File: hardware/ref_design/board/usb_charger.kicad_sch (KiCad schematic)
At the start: 34 parts, among them J1 TYPE-C-31-M-12, J2 53261-0271, Q2 AO3401A, Q4 2N7002, U1 SRV05-4, U2 TP4056-42-ESOP8

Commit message: ref_design: U1 is hongjiacheng's SRV05-4A (C20615829), a Preferred part
Same pinout as Semtech's SRV05-4.TCT (C13612, Extended), 1.0 pF to GND, 15 kV contact and
air; drops a $3-an-order setup fee. pin_review/u1.json re-checked against its datasheet
(check_pins PASS); check_netlist PASS. The board needs no copper change.

Co-Authored-By: Claude Opus 5.5 <noreply@anthropic.com>
Claude-Session: https://claude.ai/code/session_01NxPKqL46d94oRzrtCbFjri
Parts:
- U1: LCSC C13612 -> C20615829; MPN SRV05-4.TCT -> SRV05-4A; Manufacturer Semtech -> Zhuhai Hongjiacheng
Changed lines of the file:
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@@
 			)
 		)
-		(property "LCSC" "C13612"
+		(property "LCSC" "C20615829"
 			(at 73.66 101.6 0)
 			(hide yes)
@@
 			)
 		)
-		(property "MPN" "SRV05-4.TCT"
+		(property "MPN" "SRV05-4A"
 			(at 73.66 101.6 0)
 			(hide yes)
@@
 			)
 		)
-		(property "Manufacturer" "Semtech"
+		(property "Manufacturer" "Zhuhai Hongjiacheng"
 			(at 73.66 101.6 0)
 			(hide yes)

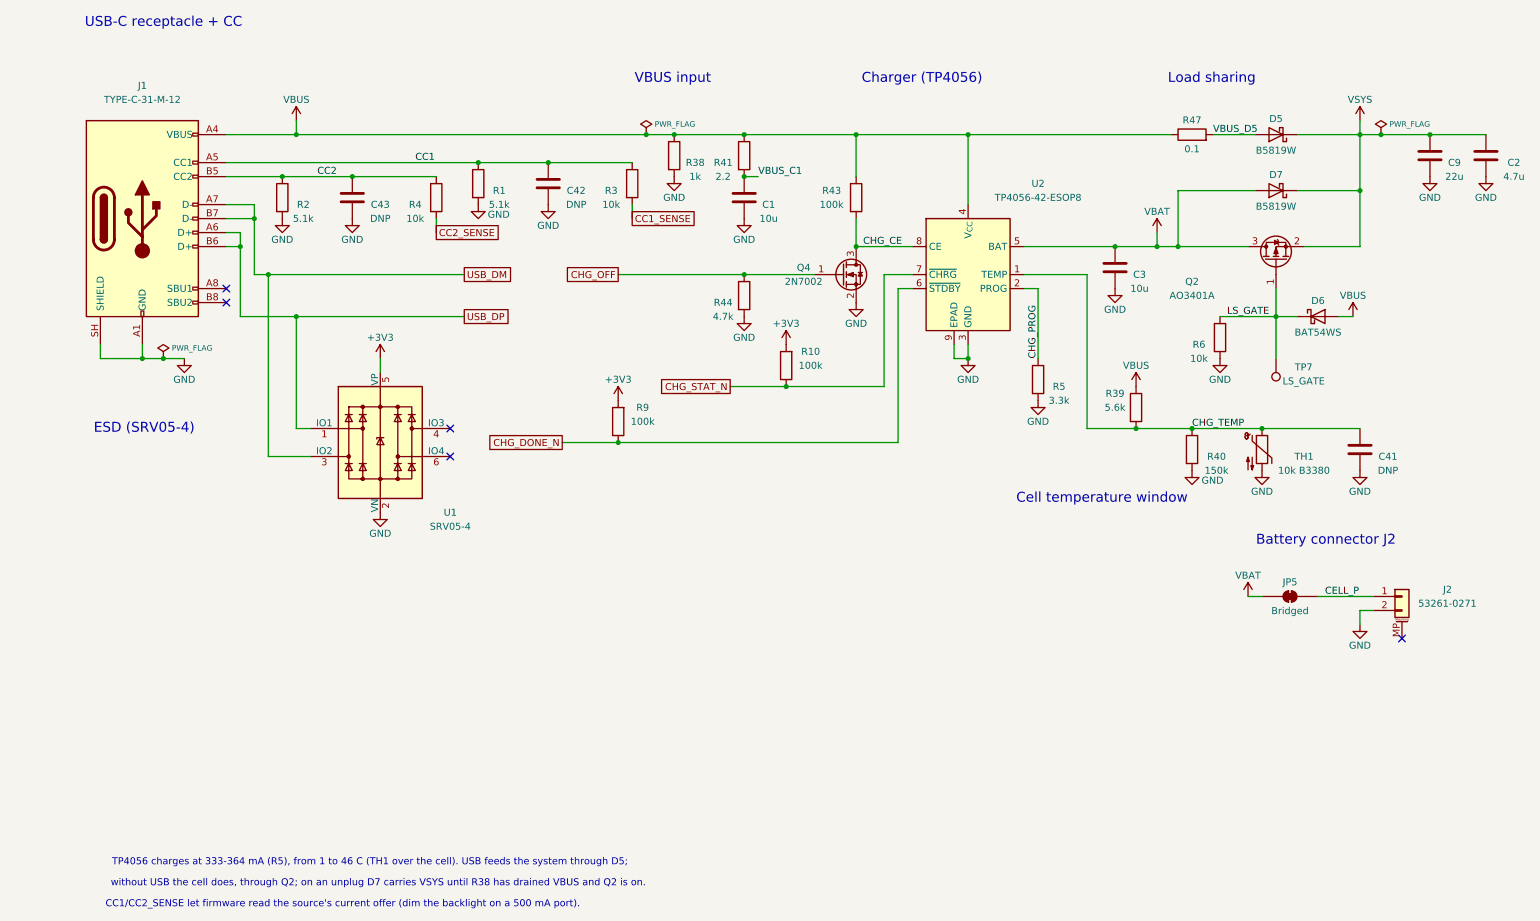
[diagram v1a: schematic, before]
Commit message: WIP: row 19 with shift registers and rows 1, 4, 16; 2 nets unrouted
The cell in a 54.0 x 37.0 mm hole, no speaker, every machine-placed part on
the top. New since the last WIP: each seat's D-pad and A/B/X/Y through a
74HC165 (SN74HC165PWR, chained, SR_PL/SR_CLK/SR_DATA on GPIO28-30, 10k
arrays); seat 2's Start powers on too (D8, R62, Q7, R63; P2_START on
GPIO34); Start/Select on 4 mm metal dome footprints; the BQ24073 power-path
charger in place of the TP4056 and its load sharing (pin reviews written);
the LDO beside the core; side screws at case (+-31.4, +-36); J1 at case
y -11. GPIO8 and GPIO11 (audio) unconnected.

Checks: check_netlist, check_pins and ERC pass (0). DRC: 0 errors, 8
cosmetic silkscreen warnings, 2 unconnected: QSPI_SS (U4 pin 75 to its
3.5 mm stub) and P1_SELECT (U4 pin 44 to SW20). check_fit: 17, all from
the case not knowing the moved screws, J1 and the dome vents yet.

Co-Authored-By: Claude Opus 5.5 <noreply@anthropic.com>
Claude-Session: https://claude.ai/code/session_01Y3mFMxLYqNeyyedvbYuRwX
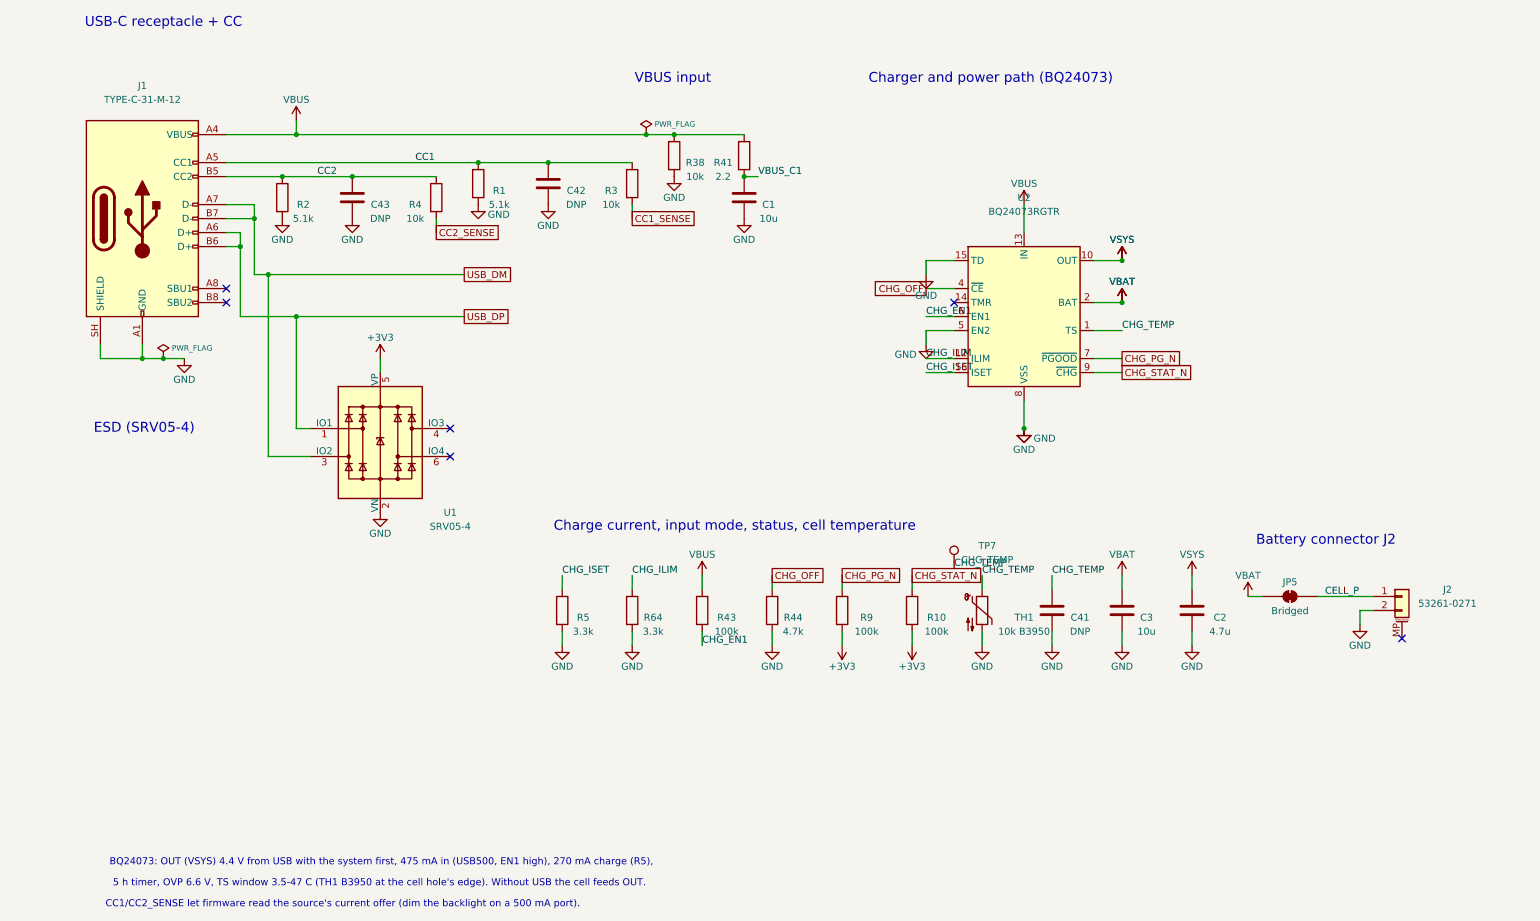
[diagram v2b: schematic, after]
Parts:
- removed C9: 22u, Capacitor_SMD:C_0805_2012Metric, symbol Device:C
- removed D5, D7: B5819W, Diode_SMD:D_SOD-123, symbol Device:D_Schottky
- removed D6: BAT54WS, Diode_SMD:D_SOD-323, symbol Device:D_Schottky
- removed Q2: AO3401A, Package_TO_SOT_SMD:SOT-23, symbol Transistor_FET:AO3401A
- removed Q4: 2N7002, Package_TO_SOT_SMD:SOT-23, symbol Transistor_FET:2N7002
- removed R39: 5.6k, Resistor_SMD:R_0402_1005Metric, symbol Device:R
- removed R40: 150k, Resistor_SMD:R_0402_1005Metric, symbol Device:R
- removed R47: 0.1, Resistor_SMD:R_1206_3216Metric, symbol Device:R
- removed R6: 10k, Resistor_SMD:R_0402_1005Metric, symbol Device:R
- added R64: 3.3k, Resistor_SMD:R_0402_1005Metric, symbol Device:R
- R38: value 1k -> 10k; footprint Resistor_SMD:R_0603_1608Metric -> Resistor_SMD:R_0402_1005Metric; LCSC C21190 -> C25744; MPN 0603WAF1001T5E -> 0402WGF1002TCE
- TH1: value 10k B3380 -> 10k B3950; LCSC C77131 -> C95939; MPN NCP15XH103F03RC -> SDNT1005X103F3950FTF; Manufacturer Murata -> Sunlord
- TP7: value LS_GATE -> CHG_TEMP
- U2: value TP4056-42-ESOP8 -> BQ24073RGTR; footprint battler:SOIC-8-1EP_3.9x4.9mm_P1.27mm_EP2.41x3.3mm_ThermalVias_0.3mm -> Package_DFN_QFN:VQFN-16-1EP_3x3mm_P0.5mm_EP1.68x1.68mm; symbol Battery_Management:TP4056-42-ESOP8 -> Battery_Management:BQ24073RGT; LCSC C16581 -> C15220; MPN TP4056-42-ESOP8 -> BQ24073RGTR; Manufacturer TOPPOWER -> Texas Instruments
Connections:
- net LS_GATE is gone; now on net CHG_TEMP: TP7.1
- net CHG_OFF: now also U2.4 (~{CE})
- net CHG_STAT_N: now also U2.9 (~{CHG}); no longer U2.7 (~{CHRG})
- net GND: now also U2.15 (TD), U2.17 (VSS), U2.5 (EN2), U2.8 (VSS), R64.2; no longer U2.3 (GND), U2.9 (EPAD)
- net VBAT: now also U2.2 (BAT), U2.3 (BAT); no longer U2.5 (BAT)
- net VBUS: now also U2.13 (IN); no longer U2.4 (V_{CC})
- net VSYS: now also U2.10 (OUT), U2.11 (OUT)
- net CHG_CE renamed CHG_EN1
- net CHG_EN1: now also U2.6 (EN1); no longer U2.8 (CE)
- net CHG_DONE_N renamed CHG_PG_N
- net CHG_PG_N: now also U2.7 (~{PGOOD}); no longer U2.6 (~{STDBY})
- net CHG_PROG renamed CHG_ISET
- net CHG_ISET: now also U2.16 (ISET); no longer U2.2 (PROG)
- new net CHG_ILIM: R64.1, U2.12 (ILIM)
- no-connect marks 5 -> 6
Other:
- note added: "5 h timer, OVP 6.6 V, TS window 3.5-47 C (TH1 B3950 at the cell hole's edge). Without USB the cell feeds OUT."
- note added: "BQ24073: OUT (VSYS) 4.4 V from USB with the system first, 475 mA in (USB500, EN1 high), 270 mA charge (R5),"
- note added: "Charge current, input mode, status, cell temperature"
- note added: "Charger and power path (BQ24073)"
- note removed: "Cell temperature window"
- note removed: "Charger (TP4056)"
- note removed: "Load sharing"
- note removed: "TP4056 charges at 333-364 mA (R5), from 1 to 46 C (TH1 over the cell). USB feeds the system through D5;"
- note removed: "without USB the cell does, through Q2; on an unplug D7 carries VSYS until R38 has drained VBUS and Q2 is on."
- moved on the sheet: C2, C3, C41, R10, R43, R44, R5, R9, TH1, TP7

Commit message: ref_design: U1 back to Semtech's SRV05-4.TCT, U3 the RT9013-33GB (JLC stock, no pre-orders)
For a 30-board JLC order with no pre-ordered parts (Alex, 2026-10-22):
- U1 USB ESD: SRV05-4A C20615829 -> Semtech SRV05-4.TCT C13612 (Extended, about 102k in
  stock). Same pinout per Semtech's datasheet (I/O 1, 3, 4, 6; GND 2; REF 5). JLC's
  footprint for C13612 is KiCad's SOT-23-6 turned 180 degrees: assembly.md says so.
- U3 3V3 LDO: ME6211C33M5G-N C82942 -> Richtek RT9013-33GB C47773 (Extended, about 311k).
  Same SOT-23-5 pinout (DS9013-10: pin 4 NC, no BP on this revision). VIN 5.5 V vs VSYS
  <= 4.5 V (BQ24073 OUT 4.3-4.5 V); EN 1.6 V high, 6 V absolute; 1 uF minimum caps.
  Same JLC footprint as C82942.
- J5/J6 not swapped: the Megastar ZX-SH1.0-3PWT clone's land pattern and body differ from
  the SM03B-SRSS-TB footprint (reported, not changed).

design.py, pin reviews, sheet headings, docs; sync_pcb now copies the value too. The board
took the new fields through sync_pcb only: copper unchanged, DRC 0 errors, 0 unconnected,
0 parity issues.

Co-Authored-By: Claude Opus 5.5 <noreply@anthropic.com>
Claude-Session: https://claude.ai/code/session_01Y3mFMxLYqNeyyedvbYuRwX
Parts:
- U1: LCSC C20615829 -> C13612; MPN SRV05-4A -> SRV05-4.TCT; Manufacturer Zhuhai Hongjiacheng -> Semtech
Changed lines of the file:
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@@
 			)
 		)
-		(property "LCSC" "C20615829"
+		(property "LCSC" "C13612"
 			(at 73.66 101.6 0)
 			(hide yes)
@@
 			)
 		)
-		(property "MPN" "SRV05-4A"
+		(property "MPN" "SRV05-4.TCT"
 			(at 73.66 101.6 0)
 			(hide yes)
@@
 			)
 		)
-		(property "Manufacturer" "Zhuhai Hongjiacheng"
+		(property "Manufacturer" "Semtech"
 			(at 73.66 101.6 0)
 			(hide yes)

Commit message: ref_design levers: pins facing their nets, no REV straps, no UART, debug buttons and latch parts out of the strips
An experiment for Alex (not on ref-design-cellcut): make the board easier to route without
changing its size.
1. GPIOs: AUDIO_PWM 8 -> 31 (PWM7 B), AMP_EN 11 -> 34, BL_PWM 44 -> 28 (PWM6 A), PWR_HOLD
   2 -> 44, P2_START 34 -> 2, P2_SELECT 9 -> 4, SR_PL 28 -> 19 (datasheet Table 3 checked;
   U4's pin review updated)
2. REV0-REV3 and R48-R51 removed (the revision stays on the silkscreen)
3. J6 (UART) and C41 removed; SW18/SW19 out of the left strip into the left bezel below H4
   (U3 and its caps 2 mm down, JP1 below the core)
4. The latch's strip parts (Q1, R16, R15, C47, TP6, D8, Q7, R62, R63) up past the hole's
   top edge under seat 2's deck; C42 to the right bezel
tools/strip_load.py counts nets through each strip: 11/15 -> 8/11, parts 8/16 -> 3/5.
Routed clean on the first finished attempt (seed 3, 4.2 min); check_pcb and check_fit pass.

Co-Authored-By: Claude Opus 5.5 <noreply@anthropic.com>
Claude-Session: https://claude.ai/code/session_01Y3mFMxLYqNeyyedvbYuRwX
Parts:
- removed C41: DNP, Capacitor_SMD:C_1206_3216Metric, symbol Device:C
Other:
- moved on the sheet: C2, C3

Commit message: ref_design V&V round 3, schematic: R61 3.74k (DEC-31), R14 47k and R43 220k with no clamp (DEC-17), RN1-RN4 47k (DEC-24), U10 buffer on VBAT_SENSE, 10k B4460 NTC for TH1, J4 JST SH, pin reviews
Co-Authored-By: Claude Sonnet 5.5 <noreply@anthropic.com>
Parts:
- R43: value 100k -> 220k; LCSC C25741 -> C25767; MPN 0402WGF1003TCE -> 0402WGF2203TCE
- TH1: value 10k B3950 -> 10k B4460; footprint Resistor_SMD:R_0402_1005Metric -> Resistor_SMD:R_0805_2012Metric; LCSC C95939 -> C525375; MPN SDNT1005X103F3950FTF -> TCTR0805F10K0F4460T; Manufacturer Sunlord -> Resistor.Today
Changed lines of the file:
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@@
 			)
 		)
-		(property "Value" "100k"
+		(property "Value" "220k"
 			(at 136.525 135.89 0)
 			(show_name no)
@@
 			)
 		)
-		(property "LCSC" "C25741"
+		(property "LCSC" "C25767"
 			(at 132.08 132.08 0)
 			(hide yes)
@@
 			)
 		)
-		(property "MPN" "0402WGF1003TCE"
+		(property "MPN" "0402WGF2203TCE"
 			(at 132.08 132.08 0)
 			(hide yes)
@@
 			)
 		)
-		(property "Value" "10k B3950"
+		(property "Value" "10k B4460"
 			(at 190.5 135.89 0)
 			(show_name no)
@@
 			)
 		)
-		(property "Footprint" "Resistor_SMD:R_0402_1005Metric"
+		(property "Footprint" "Resistor_SMD:R_0805_2012Metric"
 			(at 182.88 132.08 0)
 			(hide yes)
@@
 			)
 		)
-		(property "LCSC" "C95939"
+		(property "LCSC" "C525375"
 			(at 182.88 132.08 0)
 			(hide yes)
@@
 			)
 		)
-		(property "MPN" "SDNT1005X103F3950FTF"
+		(property "MPN" "TCTR0805F10K0F4460T"
 			(at 182.88 132.08 0)
 			(hide yes)
@@
 			)
 		)
-		(property "Manufacturer" "Sunlord"
+		(property "Manufacturer" "Resistor.Today"
 			(at 182.88 132.08 0)
 			(hide yes)

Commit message: ref_design ESP32-S3 placement: module, microSD slot, nearest-legal-spot search for the new parts (tools/place_new.py), cell hole 38.2 x 55.2 (V&V C1), U2 on TI's RGT0016C land (P3), net classes for CELL_P, AMP_VDD, VBUS_C1 (P4), comb keep-out 2.9 flats (B3), check_fit module body; check_fit PASS, placement DRC clean
Co-Authored-By: Claude Sonnet 5.5 <noreply@anthropic.com>
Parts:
- U2: footprint Package_DFN_QFN:VQFN-16-1EP_3x3mm_P0.5mm_EP1.68x1.68mm -> battler:VQFN-16-1EP_3x3mm_RGT0016C
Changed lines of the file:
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@@
 			)
 		)
-		(property "Footprint" "Package_DFN_QFN:VQFN-16-1EP_3x3mm_P0.5mm_EP1.68x1.68mm"
+		(property "Footprint" "battler:VQFN-16-1EP_3x3mm_RGT0016C"
 			(at 190.5 78.74 0)
 			(hide yes)
